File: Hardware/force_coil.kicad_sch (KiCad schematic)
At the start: 20 parts

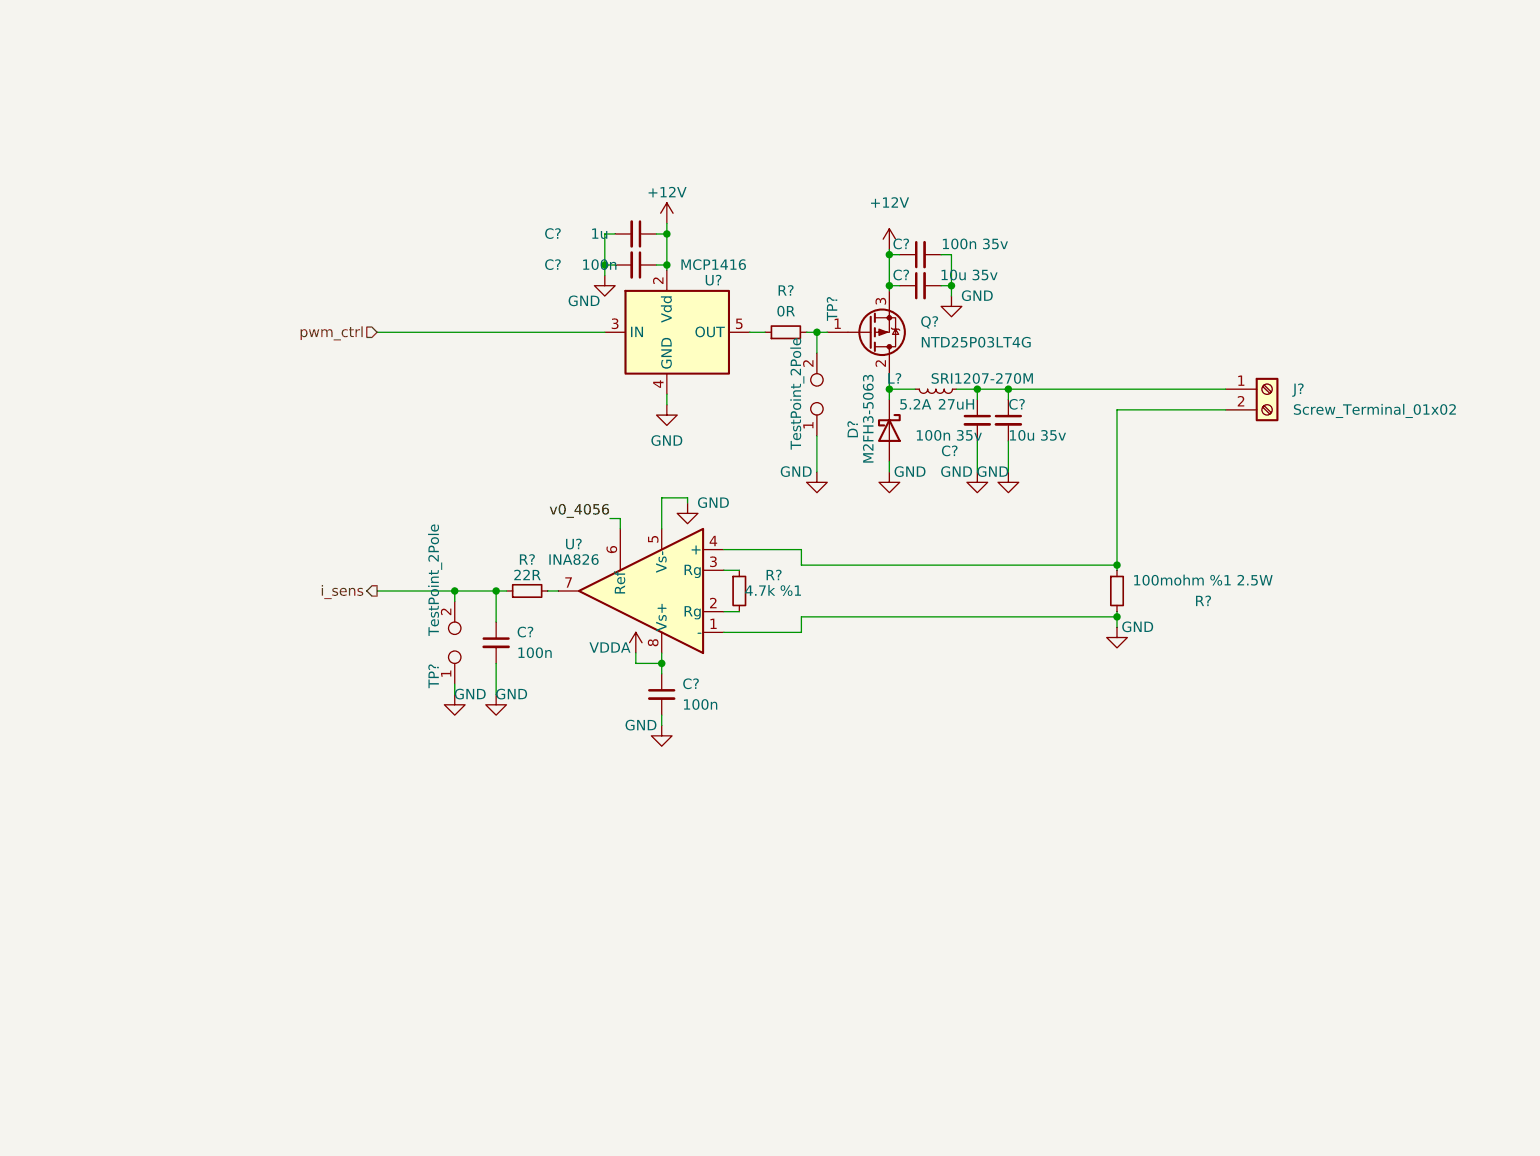
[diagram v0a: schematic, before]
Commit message: Polished coil driver. H bridge driver needs more work.
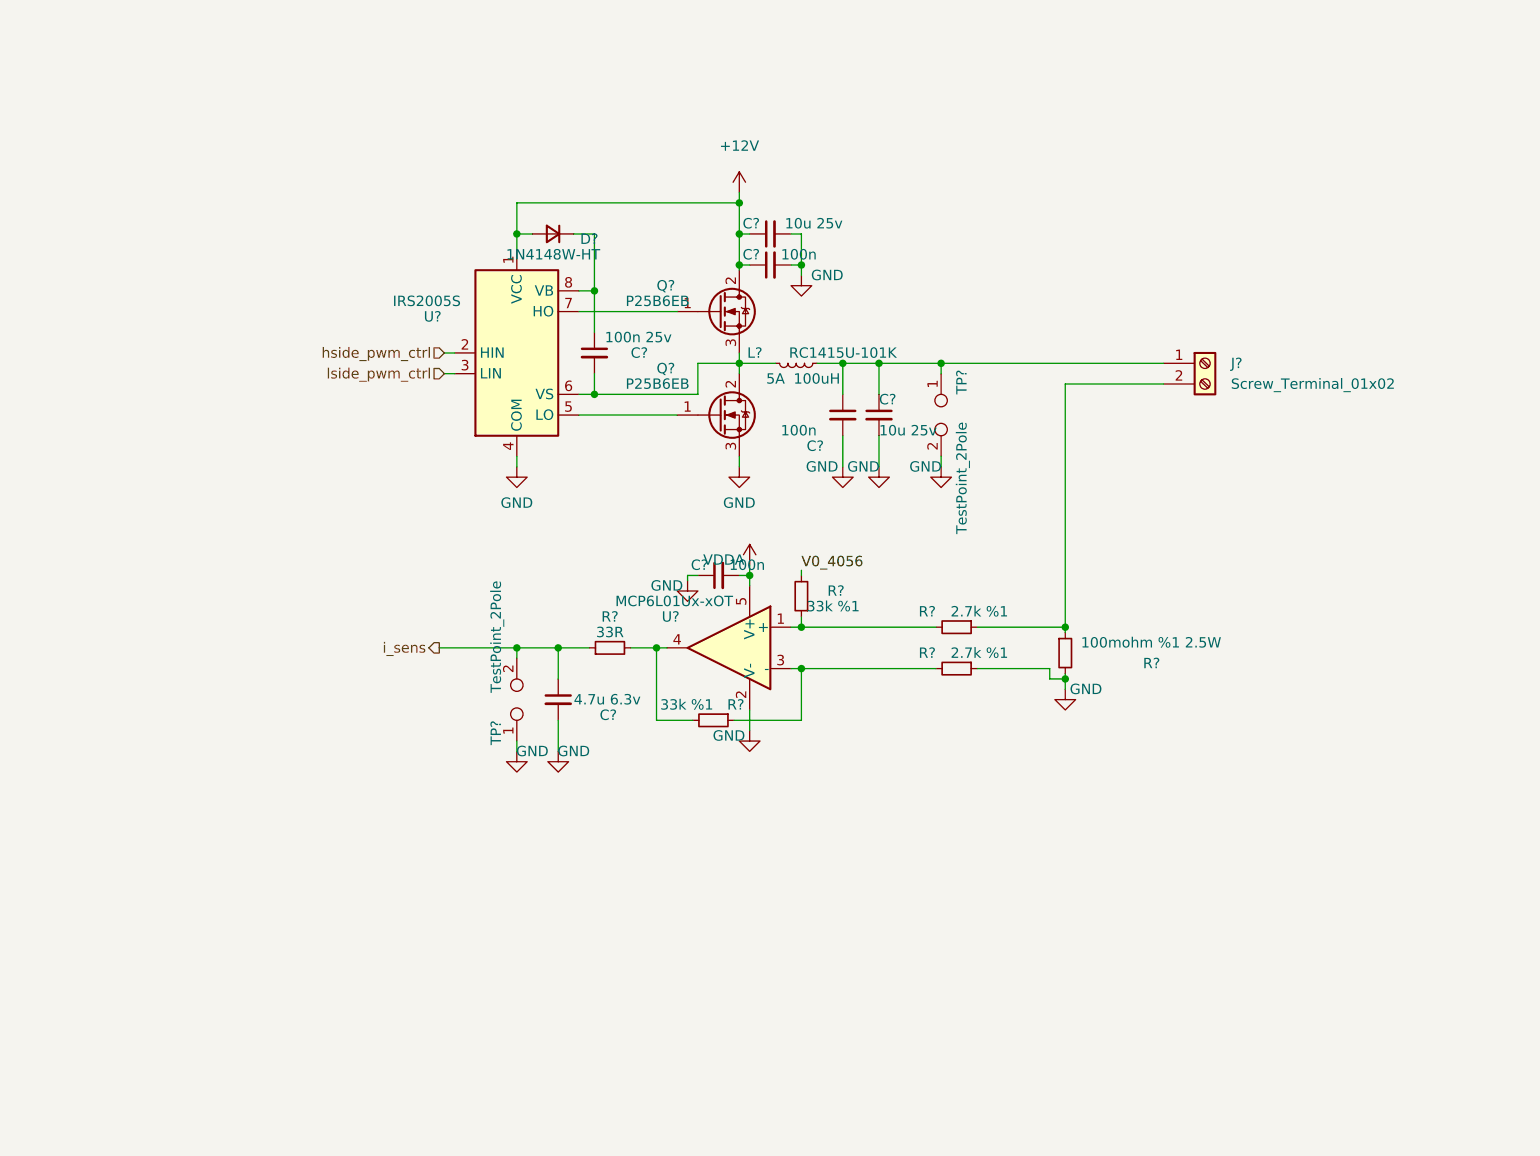
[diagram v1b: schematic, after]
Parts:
- removed C? (x2): 100n, symbol Device:C_Small
- removed C?: 10u 35v, Capacitor_SMD:C_1210_3225Metric_Pad1.33x2.70mm_HandSolder, symbol Device:C_Small
- removed C?: 100n 35v, Capacitor_SMD:C_0603_1608Metric_Pad1.08x0.95mm_HandSolder, symbol Device:C_Small
- removed C?: 1u, symbol Device:C_Small
- removed D?: M2FH3-5063, Diode_SMD:D_SMB_Handsoldering, symbol Device:D_Schottky
- removed Q?: NTD25P03LT4G, Package_TO_SOT_SMD:TO-252-3_TabPin2, symbol Device:Q_PMOS_GDS
- removed R?: 0R, symbol Device:R_Small
- removed R?: 4.7k %1, Resistor_SMD:R_0603_1608Metric_Pad0.98x0.95mm_HandSolder, symbol Device:R_Small
- removed TP?: TestPoint_2Pole, symbol Connector:TestPoint_2Pole
- removed U?: MCP1416, Package_TO_SOT_SMD:SOT-23-5, symbol Driver_FET:MCP1416
- removed U?: INA826, symbol ReflexCreations:INA826
- added C?: 10u 25v, Capacitor_SMD:C_0805_2012Metric_Pad1.18x1.45mm_HandSolder, symbol Device:C_Small
- added C? (x2): 100n, Capacitor_SMD:C_0603_1608Metric_Pad1.08x0.95mm_HandSolder, symbol Device:C_Small
- added C?: 100n 25v, Capacitor_SMD:C_0603_1608Metric_Pad1.08x0.95mm_HandSolder, symbol Device:C_Small
- added D?: 1N4148W-HT, Diode_SMD:D_SOD-123, symbol Device:D_Small
- added Q? (x2): P25B6EB, Package_TO_SOT_SMD:TO-252-3_TabPin2, symbol Device:Q_NMOS_GDS
- added R? (x2): 2.7k %1, Resistor_SMD:R_0603_1608Metric_Pad0.98x0.95mm_HandSolder, symbol Device:R_Small
- added R? (x2): 33k %1, Resistor_SMD:R_0603_1608Metric_Pad0.98x0.95mm_HandSolder, symbol Device:R_Small
- added TP?: TestPoint_2Pole, Connector_PinHeader_2.54mm:PinHeader_1x02_P2.54mm_Vertical, symbol Connector:TestPoint_2Pole
- added U?: MCP6L01Ux-xOT, Package_TO_SOT_SMD:SOT-23-5, symbol Amplifier_Operational:MCP6L01Ux-xOT
- added U?: IRS2005S, Package_SO:SOIC-8_3.9x4.9mm_P1.27mm, symbol Driver_FET:IRS2005S
- C?: value 100n -> 4.7u 6.3v; footprint (none) -> Capacitor_SMD:C_0603_1608Metric_Pad1.08x0.95mm_HandSolder; Link (none) -> https://ozdisan.com/passive-components/capacitors/smt-smd-a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; Price (none) -> 0.01079
- C?: value 100n 35v -> 100n
- C?: value 10u 35v -> 10u 25v; footprint Capacitor_SMD:C_1210_3225Metric_Pad1.33x2.70mm_HandSolder -> Capacitor_SMD:C_0805_2012Metric_Pad1.18x1.45mm_HandSolder; Link https://ozdisan.com/passive-components/capacitors/smt-smd-and-mlcc-capacitors/CL32A106KLULNNE -> https://ozdisan.com/passive-components/capacitors/smt-smd-and-mlcc-capacitors/CL21A106KAYNNNE; Price 0.17032 -> 0.04807
- J?: Link (none) -> https://ozdisan.com/connectors-and-interconnects/terminal-b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; Price (none) -> 0.10870
- L?: value SRI1207-270M -> RC1415U-101K; Current 5.2A -> 5A; Inductance 27uH -> 100uH; Link https://ozdisan.com/passive-components/inductors/fixed-inductors/SRI1207-270M -> https://ozdisan.com/passive-components/inductors/fixed-inductors/RC1415U-101K; Price 0.42573 -> 1.21707
- R?: value 22R -> 33R; footprint (none) -> Resistor_SMD:R_0603_1608Metric_Pad0.98x0.95mm_HandSolder; Link (none) -> https://ozdisan.com/passive-components/resistors/smt-smd-an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; Price (none) -> 0.00169
- TP?: footprint (none) -> Connector_PinHeader_2.54mm:PinHeader_1x02_P2.54mm_Vertical; Link (none) -> https://ozdisan.com/connectors-and-interconnects/headers/pi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; Price (none) -> 0.1293
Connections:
- net +12V: now also C?.1, C?.1, D?.2 (A), Q?.2 (D), U?.1 (VCC)
- net GND: now also C?.1, C?.2, C?.2, Q?.3 (S), R?.1, TP?.2, U?.2 (V-), U?.4 (COM)
- net VDDA: now also C?.2, U?.5 (V+)
- net at L?.2: now also C?.2, Q?.2 (D), Q?.3 (S), U?.6 (VS)
- net at J?.2 (Pin_2), R?.1: now also R?.1
- net at C?.1, C?.1, J?.1 (Pin_1)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: now also TP?.1
- net at R?.2: now also R?.2, U?.4
- new net: R?.1, R?.2, U?.1 (+)
- new net: R?.1, R?.2, U?.3 (-)
- new net: Q?.1 (G), U?.5 (LO)
- new net: Q?.1 (G), U?.7 (HO)
- new net: C?.1, D?.1 (K), U?.8 (VB)
- new net V0_4056: R?.2
- new net hside_pwm_ctrl: U?.2 (HIN)
- new net lside_pwm_ctrl: U?.3 (LIN)
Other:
- moved on the sheet: C?, J?, L?, R?, TP?

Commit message: Changes about piezo transducer driver
+ Regarding measurement of piezo transducer impedance, driver circuit is updated.(-+15v). Besides circuit is updated. But yet to be simulated for new resistance values.
+ Most cost efficient analog design(up to now) is created. Noise free enough, but nothing more.
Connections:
- net +12V renamed +15V
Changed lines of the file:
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@@
     (effects (font (size 1.27 1.27)) (justify right))
+  )
+  (symbol (lib_id "power:+15V") (at 140.335 69.215 0) (unit 1)
+    (in_bom yes) (on_board yes) (fields_autoplaced)
+    (property "Reference" "#PWR?" (id 0) (at 140.335 73.025 0)
+      (effects (font (size 1.27 1.27)) hide)
+    )
+    (property "Value" "+15V" (id 1) (at 140.335 63.5 0))
+    (property "Footprint" "" (id 2) (at 140.335 69.215 0)
+      (effects (font (size 1.27 1.27)) hide)
+    )
+    (property "Datasheet" "" (id 3) (at 140.335 69.215 0)
+      (effects (font (size 1.27 1.27)) hide)
+    )
+    (pin "1")
   )
   (symbol (lib_id "Device:C_Small") (at 118.11 131.445 0) (unit 1)
@@
     (pin "2")
   )
-  (symbol (lib_id "power:+12V") (at 140.335 69.215 0) (unit 1)
-    (in_bom yes) (on_board yes) (fields_autoplaced)
-    (property "Reference" "#PWR?" (id 0) (at 140.335 73.025 0)
-      (effects (font (size 1.27 1.27)) hide)
-    )
-    (property "Value" "+12V" (id 1) (at 140.335 63.5 0))
-    (property "Footprint" "" (id 2) (at 140.335 69.215 0)
-      (effects (font (size 1.27 1.27)) hide)
-    )
-    (property "Datasheet" "" (id 3) (at 140.335 69.215 0)
-      (effects (font (size 1.27 1.27)) hide)
-    )
-    (pin "1")
-  )
   (symbol (lib_id "Device:R_Small") (at 137.16 133.985 270) (unit 1)

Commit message: Completed schematic and PCB.
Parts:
- removed C?: 4.7u 6.3v, Capacitor_SMD:C_0603_1608Metric_Pad1.08x0.95mm_HandSolder, symbol Device:C_Small
- removed C?: 100n, Capacitor_SMD:C_0603_1608Metric_Pad1.08x0.95mm_HandSolder, symbol Device:C_Small
- removed J?: Screw_Terminal_01x02, symbol Connector:Screw_Terminal_01x02
- removed R? (x2): 2.7k %1, Resistor_SMD:R_0603_1608Metric_Pad0.98x0.95mm_HandSolder, symbol Device:R_Small
- removed R?: 33R, Resistor_SMD:R_0603_1608Metric_Pad0.98x0.95mm_HandSolder, symbol Device:R_Small
- removed R? (x2): 33k %1, Resistor_SMD:R_0603_1608Metric_Pad0.98x0.95mm_HandSolder, symbol Device:R_Small
- removed TP?: TestPoint_2Pole, Connector_PinHeader_2.54mm:PinHeader_1x02_P2.54mm_Vertical, symbol Connector:TestPoint_2Pole
- removed U?: MCP6L01Ux-xOT, Package_TO_SOT_SMD:SOT-23-5, symbol Amplifier_Operational:MCP6L01Ux-xOT
- added C5: 1u, Capacitor_SMD:C_0603_1608Metric_Pad1.08x0.95mm_HandSolder, symbol Device:C_Small
- added C56, C58: 100n, Capacitor_SMD:C_0603_1608Metric_Pad1.08x0.95mm_HandSolder, symbol Device:C_Small
- added C61: 12n %5, Capacitor_SMD:C_0805_2012Metric_Pad1.18x1.45mm_HandSolder, symbol Device:C_Small
- added C62: 1n, Capacitor_SMD:C_0603_1608Metric_Pad1.08x0.95mm_HandSolder, symbol Device:C_Small
- added C63: 10n %5, Capacitor_SMD:C_0603_1608Metric_Pad1.08x0.95mm_HandSolder, symbol Device:C_Small
- added J6: DG301-5-0-02P-12-00AH, conn:DG301-5.0-02P-12-00AH, symbol Connector:Screw_Terminal_01x02
- added R10, R9: 10k %1, Resistor_SMD:R_0603_1608Metric_Pad0.98x0.95mm_HandSolder, symbol Device:R_Small
- added R65, R66: 8.2R, Resistor_SMD:R_0603_1608Metric_Pad0.98x0.95mm_HandSolder, symbol Device:R_Small
- added R67: 56R %1, Resistor_SMD:R_0603_1608Metric_Pad0.98x0.95mm_HandSolder, symbol Device:R_Small
- added R68: 33.2k %1, Resistor_SMD:R_0603_1608Metric_Pad0.98x0.95mm_HandSolder, symbol Device:R_Small
- added R69: 47R, Resistor_SMD:R_0603_1608Metric_Pad0.98x0.95mm_HandSolder, symbol Device:R_Small
- added R70, R74: 4.87k %1, Resistor_SMD:R_0603_1608Metric_Pad0.98x0.95mm_HandSolder, symbol Device:R_Small
- added R71, R73: 14.3k %1, Resistor_SMD:R_0603_1608Metric_Pad0.98x0.95mm_HandSolder, symbol Device:R_Small
- added R72: 57.6k %1, Resistor_SMD:R_0603_1608Metric_Pad0.98x0.95mm_HandSolder, symbol Device:R_Small
- added TP13, TP14: TestPoint_2Pole, Connector_PinHeader_2.54mm:PinHeader_1x02_P2.54mm_Vertical, symbol Connector:TestPoint_2Pole
- added U10: MCP6282, Package_SO:SOIC-8_3.9x4.9mm_P1.27mm, symbol Device:Opamp_Dual
- C57: renamed from C?; value 100n 25v -> 100n
- D5: renamed from D?; value 1N4148W-HT -> 1N4148W
- L1: renamed from L?; footprint (none) -> inductor:RC1415U-101K
- Q13, Q14: renamed from Q?; footprint Package_TO_SOT_SMD:TO-252-3_TabPin2 -> Package_TO_SOT_SMD:TO-252-2
- TP15: renamed from TP?; Link https://ozdisan.com/connectors-and-interconnects/headers/pin-headers/C2100-02ASGAS0R -> https://ozdisan.com/connectors-and-interconnects/headers/pin-headers/L-KLS1-207-1-02-S
- gave numbers to parts that had none: 6
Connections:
- net GND: now also C5.1, C56.2, C58.1, C62.2, C63.1, R10.2, R70.2, TP13.1, TP14.2, U10.4 (V-)
- net VDDA: now also C58.2, R9.1, U10.8 (V+)
- net at R75.1: now also J6.1 (Pin_1), R74.2
- net at C64.1, C65.1, L1.1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: now also J6.2 (Pin_2)
- net at C57.2, L1.2, Q13.3 (S)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: now also R69.1, TP14.1
- net at Q14.1 (G): now also R66.1; no longer U9.5 (LO)
- net at Q13.1 (G): now also R65.1; no longer U9.7 (HO)
- net hside_pwm_ctrl renamed PWM
- net lside_pwm_ctrl renamed nPWM
- new net: C63.2, R72.1, U10.3 (+)
- new net: C61.2, R72.2, R73.2, R74.1
- new net: C62.1, R69.2
- new net: C61.1, R67.2, R68.2, U10.1
- new net: R68.1, R70.1, R71.2, U10.2 (-)
- new net: C5.2, R10.1, R9.2, U10.5 (+)
- new net: R71.1, R73.1, U10.6 (-), U10.7
- new net: R66.2, U9.5 (LO)
- new net: R65.2, U9.7 (HO)
- new net ISENS: C56.1, R67.1, TP13.2
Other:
- moved on the sheet: C57, C59, C60, C64, C65, D5, L1, Q13, Q14, R75, TP15, U9

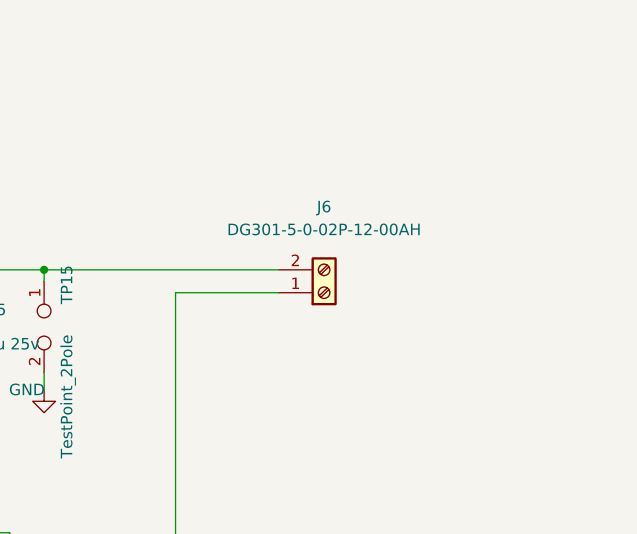
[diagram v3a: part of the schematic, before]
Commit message: Few coonector footprint modifications and silkscreen additions to them.
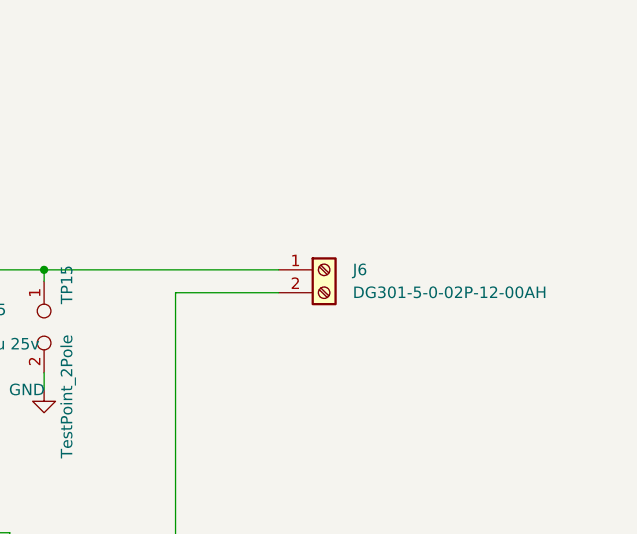
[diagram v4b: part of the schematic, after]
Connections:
- net at R74.2, R75.1: now also J6.2 (Pin_2); no longer J6.1 (Pin_1)
- net at C64.1, C65.1, L1.1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: now also J6.1 (Pin_1); no longer J6.2 (Pin_2)
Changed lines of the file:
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@@
     (pin "1")
   )
-  (symbol (lib_id "Connector:Screw_Terminal_01x02") (at 203.835 78.105 0) (mirror x) (unit 1)
+  (symbol (lib_id "Connector:Screw_Terminal_01x02") (at 203.835 75.565 0) (unit 1)
     (in_bom yes) (on_board yes) (fields_autoplaced)
-    (property "Reference" "J6" (id 0) (at 203.835 68.58 0))
-    (property "Value" "DG301-5-0-02P-12-00AH" (id 1) (at 203.835 71.12 0))
-    (property "Footprint" "conn:DG301-5.0-02P-12-00AH" (id 2) (at 203.835 78.105 0)
+    (property "Reference" "J6" (id 0) (at 207.01 75.5649 0)
+      (effects (font (size 1.27 1.27)) (justify left))
+    )
+    (property "Value" "DG301-5-0-02P-12-00AH" (id 1) (at 207.01 78.1049 0)
+      (effects (font (size 1.27 1.27)) (justify left))
+    )
+    (property "Footprint" "conn:DG301-5.0-02P-12-00AH" (id 2) (at 203.835 75.565 0)
       (effects (font (size 1.27 1.27)) hide)
     )
-    (property "Datasheet" "~" (id 3) (at 203.835 78.105 0)
+    (property "Datasheet" "~" (id 3) (at 203.835 75.565 0)
       (effects (font (size 1.27 1.27)) hide)
     )
-    (property "Link" "https://ozdisan.com/connectors-and-interconnects/terminal-blocks/pcb-terminal-blocks/DG301-5-0-02P-12-00AH" (id 4) (at 203.835 78.105 0)
+    (property "Link" "https://ozdisan.com/connectors-and-interconnects/terminal-blocks/pcb-terminal-blocks/DG301-5-0-02P-12-00AH" (id 4) (at 203.835 75.565 0)
       (effects (font (size 1.27 1.27)) hide)
     )
-    (property "Price" "0.11212" (id 5) (at 203.835 78.105 0)
+    (property "Price" "0.11212" (id 5) (at 203.835 75.565 0)
       (effects (font (size 1.27 1.27)) hide)
     )

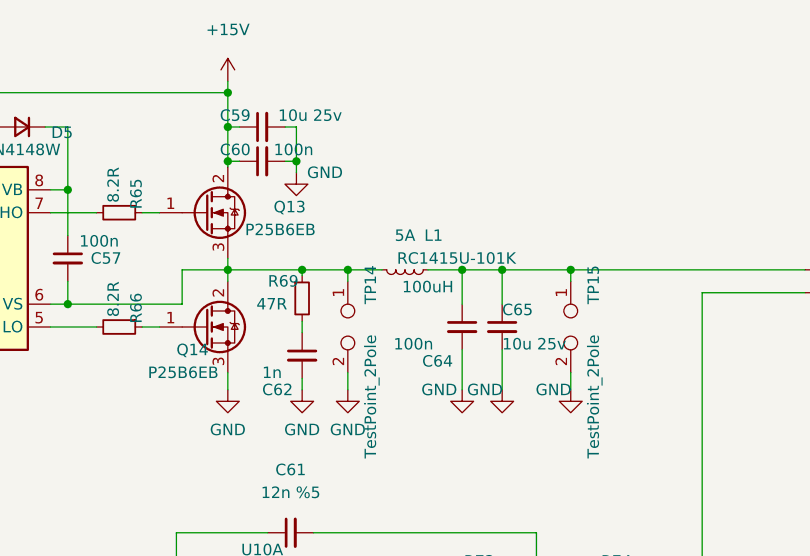
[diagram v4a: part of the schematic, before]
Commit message: Toolchain set. Timer module added. Schematic files migrated.
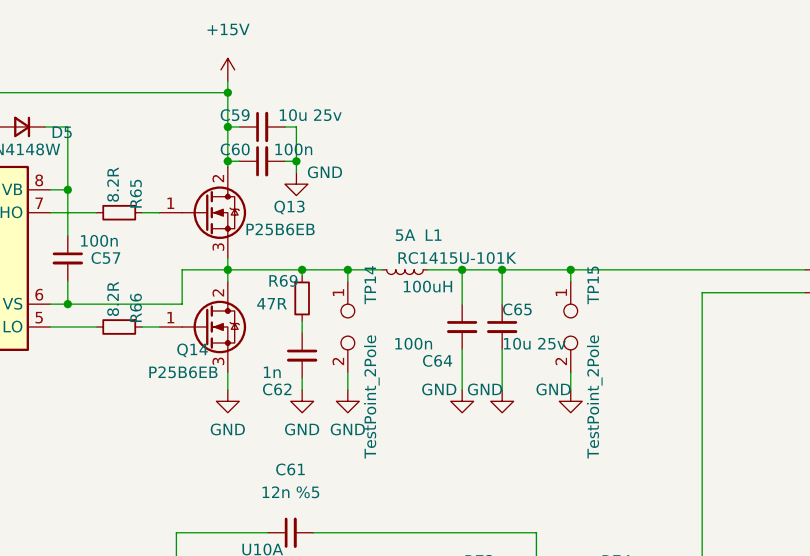
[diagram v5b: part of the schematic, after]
